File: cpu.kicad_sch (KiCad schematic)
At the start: 31 parts, among them IC901 HUC6280, IC906 LC3664BML-10

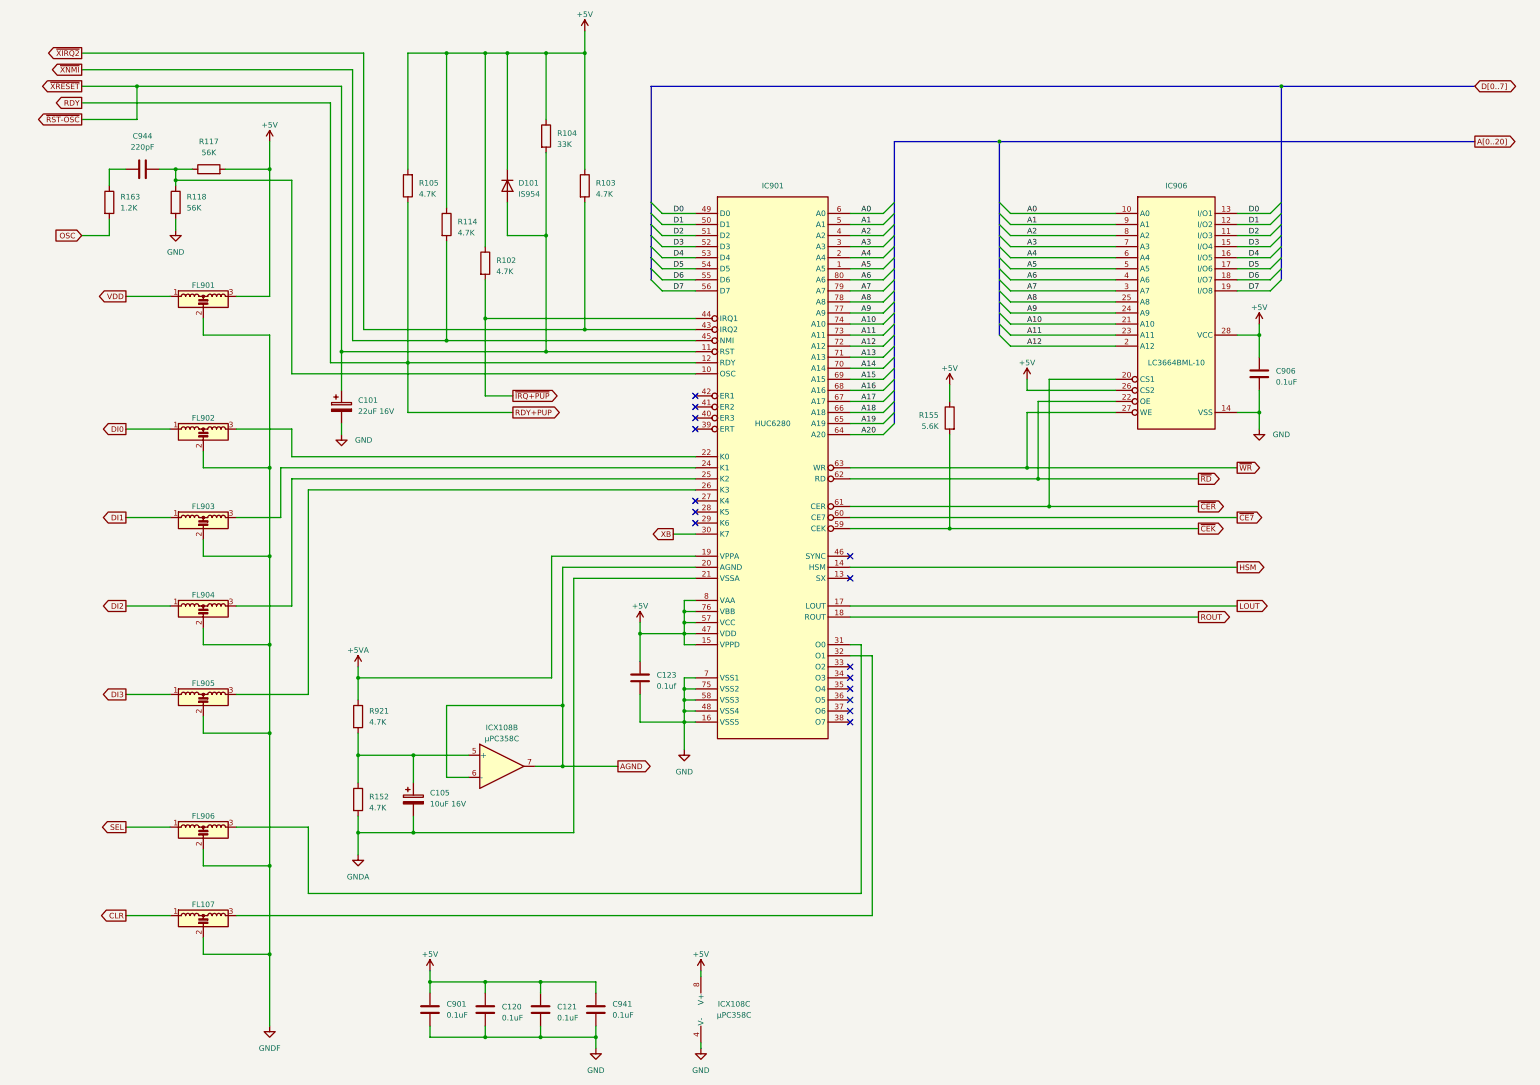
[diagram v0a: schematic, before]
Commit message: Add proper scans, redo traces.
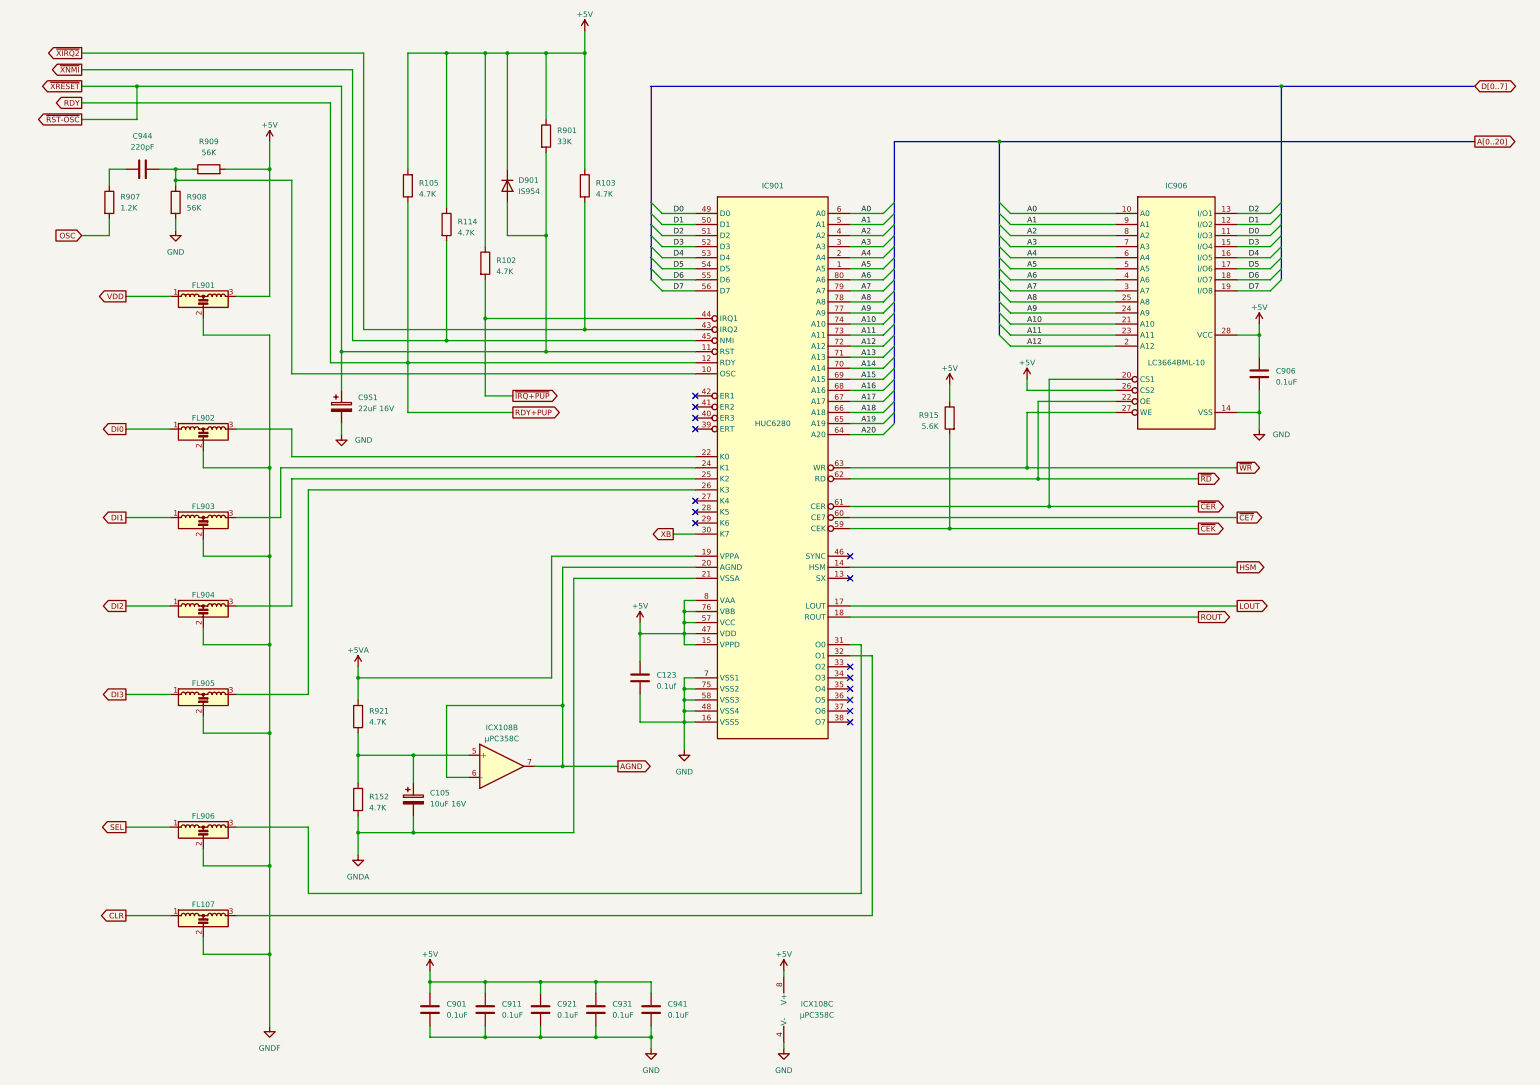
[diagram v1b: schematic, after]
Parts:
- added C921: 0.1uF, Capacitor_SMD:C_0805_2012Metric, symbol Device:C
- C951: renamed from C101; footprint A-PCENGINE:Elec_P5.00mm -> Capacitor_SMD:C_0805_2012Metric
- renumbered C120 to C911, C121 to C931, D101 to D901, R104 to R901, R163 to R907, R118 to R908, R117 to R909, R155 to R915
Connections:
- net +5V: now also C921.1
- net D0: now also IC906.11 (I/O3); no longer IC906.13 (I/O1)
- net D2: now also IC906.13 (I/O1); no longer IC906.11 (I/O3)
- net GND: now also C921.2
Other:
- moved on the sheet: C931, C941, ICX108C

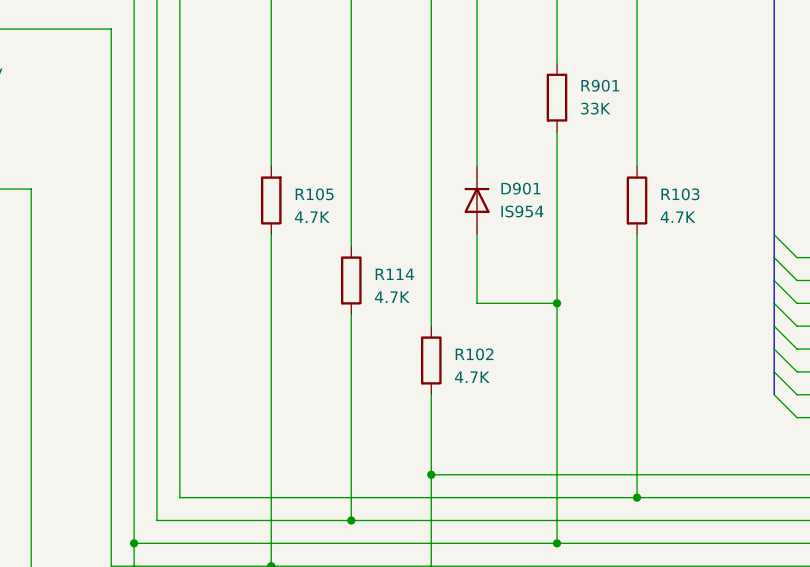
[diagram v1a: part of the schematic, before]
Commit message: IC routing mostly complete, start adding passives.
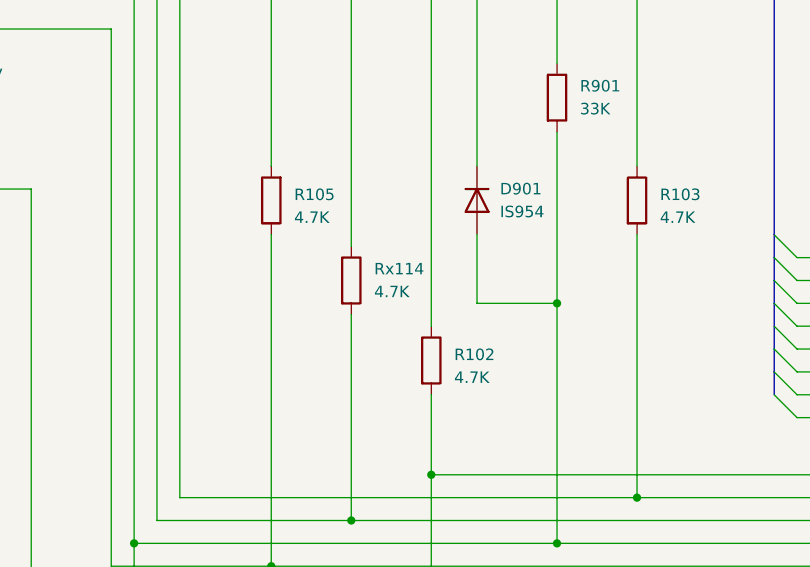
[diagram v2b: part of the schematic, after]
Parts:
- C123, C901, C906, C911, C921, C931, C941, C944, C951: footprint Capacitor_SMD:C_0805_2012Metric -> A-PCENGINE:SMD_0805_Narrow
- R102, R103, R105, R152, R901, R907, R908, R909, R915, R921: footprint Resistor_SMD:R_0805_2012Metric -> A-PCENGINE:SMD_0805_Narrow
- Rx114: renamed from R114; footprint Resistor_SMD:R_0805_2012Metric -> A-PCENGINE:SMD_0805_Narrow
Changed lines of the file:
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@@
       (effects (font (size 1.27 1.27)) (justify left))
     )
-    (property "Footprint" "Resistor_SMD:R_0805_2012Metric" (at 113.792 199.39 90)
+    (property "Footprint" "A-PCENGINE:SMD_0805_Narrow" (at 113.792 199.39 90)
       (effects (font (size 1.27 1.27)) hide)
     )
@@
       (effects (font (size 1.27 1.27)) (justify left))
     )
-    (property "Footprint" "Resistor_SMD:R_0805_2012Metric" (at 156.972 46.99 90)
+    (property "Footprint" "A-PCENGINE:SMD_0805_Narrow" (at 156.972 46.99 90)
       (effects (font (size 1.27 1.27)) hide)
     )
@@
   (symbol (lib_id "Device:R") (at 135.89 67.31 0) (unit 1)
     (in_bom yes) (on_board yes) (dnp no) (fields_autoplaced)
-    (property "Reference" "R114" (at 138.43 66.675 0)
-      (effects (font (size 1.27 1.27)) (justify left))
-    )
-    (property "Value" "4.7K" (at 138.43 69.215 0)
-      (effects (font (size 1.27 1.27)) (justify left))
-    )
-    (property "Footprint" "Resistor_SMD:R_0805_2012Metric" (at 134.112 67.31 90)
+    (property "Reference" "Rx114" (at 138.43 66.04 0)
+      (effects (font (size 1.27 1.27)) (justify left))
+    )
+    (property "Value" "4.7K" (at 138.43 68.58 0)
+      (effects (font (size 1.27 1.27)) (justify left))
+    )
+    (property "Footprint" "A-PCENGINE:SMD_0805_Narrow" (at 134.112 67.31 90)
       (effects (font (size 1.27 1.27)) hide)
     )
@@
       (project "PCE"
         (path "/c1c718c6-a427-431e-a18b-e46f94ae8e09/1d91d06a-381a-4a70-bfc1-2abf4d159a91"
-          (reference "R114") (unit 1)
+          (reference "Rx114") (unit 1)
         )
       )
@@
       (effects (font (size 1.27 1.27)) (justify left))
     )
-    (property "Footprint" "Capacitor_SMD:C_0805_2012Metric" (at 133.0452 251.46 0)
+    (property "Footprint" "A-PCENGINE:SMD_0805_Narrow" (at 133.0452 251.46 0)
       (effects (font (size 1.27 1.27)) hide)
     )
@@
       (effects (font (size 1.27 1.27)) (justify left))
     )
-    (property "Footprint" "Resistor_SMD:R_0805_2012Metric" (at 165.862 58.42 90)
+    (property "Footprint" "A-PCENGINE:SMD_0805_Narrow" (at 165.862 58.42 90)
       (effects (font (size 1.27 1.27)) hide)
     )
@@
       (effects (font (size 1.27 1.27)) (justify right))
     )
-    (property "Footprint" "Resistor_SMD:R_0805_2012Metric" (at 128.778 58.42 90)
+    (property "Footprint" "A-PCENGINE:SMD_0805_Narrow" (at 128.778 58.42 90)
       (effects (font (size 1.27 1.27)) hide)
     )
@@
       (effects (font (size 1.27 1.27)) (justify left))
     )
-    (property "Footprint" "Capacitor_SMD:C_0805_2012Metric" (at 181.3052 175.26 0)
+    (property "Footprint" "A-PCENGINE:SMD_0805_Narrow" (at 181.3052 175.26 0)
       (effects (font (size 1.27 1.27)) hide)
     )
@@
       (effects (font (size 1.27 1.27)) (justify left))
     )
-    (property "Footprint" "Capacitor_SMD:C_0805_2012Metric" (at 158.4452 251.46 0)
+    (property "Footprint" "A-PCENGINE:SMD_0805_Narrow" (at 158.4452 251.46 0)
       (effects (font (size 1.27 1.27)) hide)
     )
@@
       (effects (font (size 1.27 1.27)) (justify left))
     )
-    (property "Footprint" "Resistor_SMD:R_0805_2012Metric" (at 143.002 76.2 90)
+    (property "Footprint" "A-PCENGINE:SMD_0805_Narrow" (at 143.002 76.2 90)
       (effects (font (size 1.27 1.27)) hide)
     )
@@
       (effects (font (size 1.27 1.27)) (justify left))
     )
-    (property "Footprint" "Resistor_SMD:R_0805_2012Metric" (at 71.882 62.23 90)
+    (property "Footprint" "A-PCENGINE:SMD_0805_Narrow" (at 71.882 62.23 90)
       (effects (font (size 1.27 1.27)) hide)
     )
@@
       (effects (font (size 1.27 1.27)) (justify left))
     )
-    (property "Footprint" "Capacitor_SMD:C_0805_2012Metric" (at 171.1452 251.46 0)
+    (property "Footprint" "A-PCENGINE:SMD_0805_Narrow" (at 171.1452 251.46 0)
       (effects (font (size 1.27 1.27)) hide)
     )
@@
       (effects (font (size 1.27 1.27)))
     )
-    (property "Footprint" "Resistor_SMD:R_0805_2012Metric" (at 81.28 56.388 90)
+    (property "Footprint" "A-PCENGINE:SMD_0805_Narrow" (at 81.28 56.388 90)
       (effects (font (size 1.27 1.27)) hide)
     )
@@
       (effects (font (size 1.27 1.27)) (justify left))
     )
-    (property "Footprint" "Resistor_SMD:R_0805_2012Metric" (at 56.642 62.23 90)
+    (property "Footprint" "A-PCENGINE:SMD_0805_Narrow" (at 56.642 62.23 90)
       (effects (font (size 1.27 1.27)) hide)
     )
@@
       (effects (font (size 1.27 1.27)))
     )
-    (property "Footprint" "Capacitor_SMD:C_0805_2012Metric" (at 69.85 53.6448 0)
+    (property "Footprint" "A-PCENGINE:SMD_0805_Narrow" (at 69.85 53.6448 0)
       (effects (font (size 1.27 1.27)) hide)
     )
@@
       (effects (font (size 1.27 1.27)) (justify left))
     )
-    (property "Footprint" "Capacitor_SMD:C_0805_2012Metric" (at 112.7252 113.03 0)
+    (property "Footprint" "A-PCENGINE:SMD_0805_Narrow" (at 112.7252 113.03 0)
       (effects (font (size 1.27 1.27)) hide)
     )
@@
       (effects (font (size 1.27 1.27)) (justify left))
     )
-    (property "Footprint" "Resistor_SMD:R_0805_2012Metric" (at 113.792 180.34 90)
+    (property "Footprint" "A-PCENGINE:SMD_0805_Narrow" (at 113.792 180.34 90)
       (effects (font (size 1.27 1.27)) hide)
     )
@@
       (effects (font (size 1.27 1.27)) (justify left))
     )
-    (property "Footprint" "Capacitor_SMD:C_0805_2012Metric" (at 183.8452 251.46 0)
+    (property "Footprint" "A-PCENGINE:SMD_0805_Narrow" (at 183.8452 251.46 0)
       (effects (font (size 1.27 1.27)) hide)
     )
@@
       (effects (font (size 1.27 1.27)) (justify left))
     )
-    (property "Footprint" "Capacitor_SMD:C_0805_2012Metric" (at 323.5452 105.41 0)
+    (property "Footprint" "A-PCENGINE:SMD_0805_Narrow" (at 323.5452 105.41 0)
       (effects (font (size 1.27 1.27)) hide)
     )
@@
       (effects (font (size 1.27 1.27)) (justify left))
     )
-    (property "Footprint" "Resistor_SMD:R_0805_2012Metric" (at 253.238 111.76 90)
+    (property "Footprint" "A-PCENGINE:SMD_0805_Narrow" (at 253.238 111.76 90)
       (effects (font (size 1.27 1.27)) hide)
     )
@@
       (effects (font (size 1.27 1.27)) (justify left))
     )
-    (property "Footprint" "Capacitor_SMD:C_0805_2012Metric" (at 145.7452 251.46 0)
-      (effects (font (size 1.27 1.27)) hide)
-    )
+    (property "Footprint" "A-PCENGINE:SMD_0805_Narrow" (at 145.7452 251.46 0)
+      (effects (font (size 1.27 1.27)) hide)
+    )
